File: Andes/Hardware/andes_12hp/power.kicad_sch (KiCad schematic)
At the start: 17 parts, among them J13 Eurorack Power, U6 LM4040LP-10, U7 L78L05_TO92

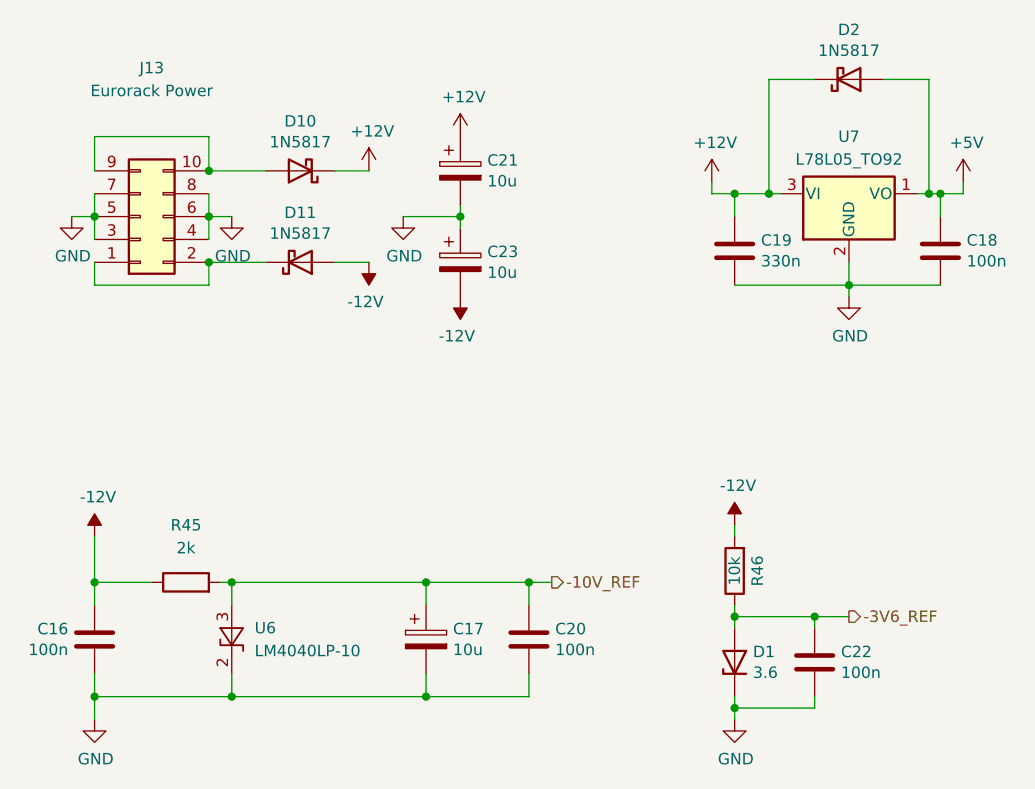
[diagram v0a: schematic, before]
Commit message: Sync changes in 8HP Andes to 12HP Andes
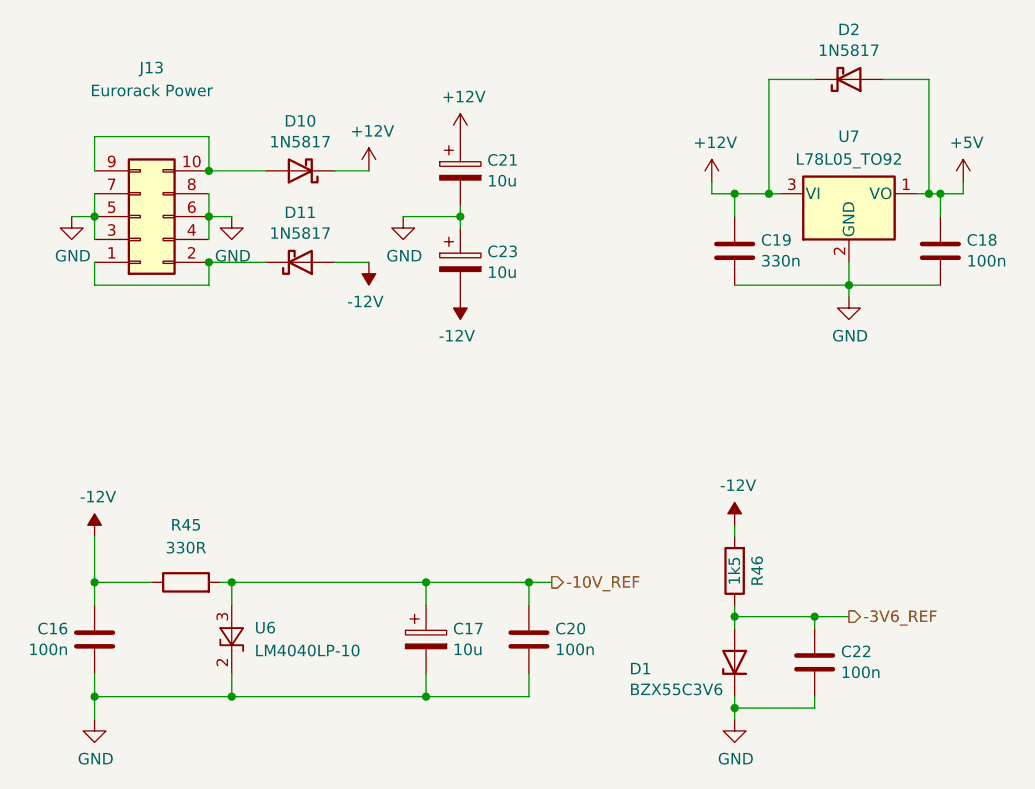
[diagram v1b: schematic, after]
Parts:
- D1: value 3.6 -> BZX55C3V6
- R45: value 2k -> 330R
- R46: value 10k -> 1k5
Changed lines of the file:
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@@
 		(dnp no)
 		(property "Reference" "D1"
-			(at 158.242 122.0216 90)
+			(at 144.526 123.9266 90)
 			(effects
 				(font
@@
 			)
 		)
-		(property "Value" "3.6"
-			(at 158.242 124.333 90)
+		(property "Value" "BZX55C3V6"
+			(at 144.526 126.238 90)
 			(effects
 				(font
@@
 			)
 		)
-		(property "Value" "10k"
+		(property "Value" "1k5"
 			(at 156.21 113.03 90)
 			(effects
@@
 			)
 		)
-		(property "Value" "2k"
+		(property "Value" "330R"
 			(at 95.25 110.49 90)
 			(effects
